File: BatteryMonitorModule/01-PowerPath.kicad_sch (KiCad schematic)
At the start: 22 parts, among them K1 G5LE-1, Q1 AO3401A, Q2 MMBT2222A, Q3 IRFZ44NPBF, Q3_DRV1 MMBT2222A

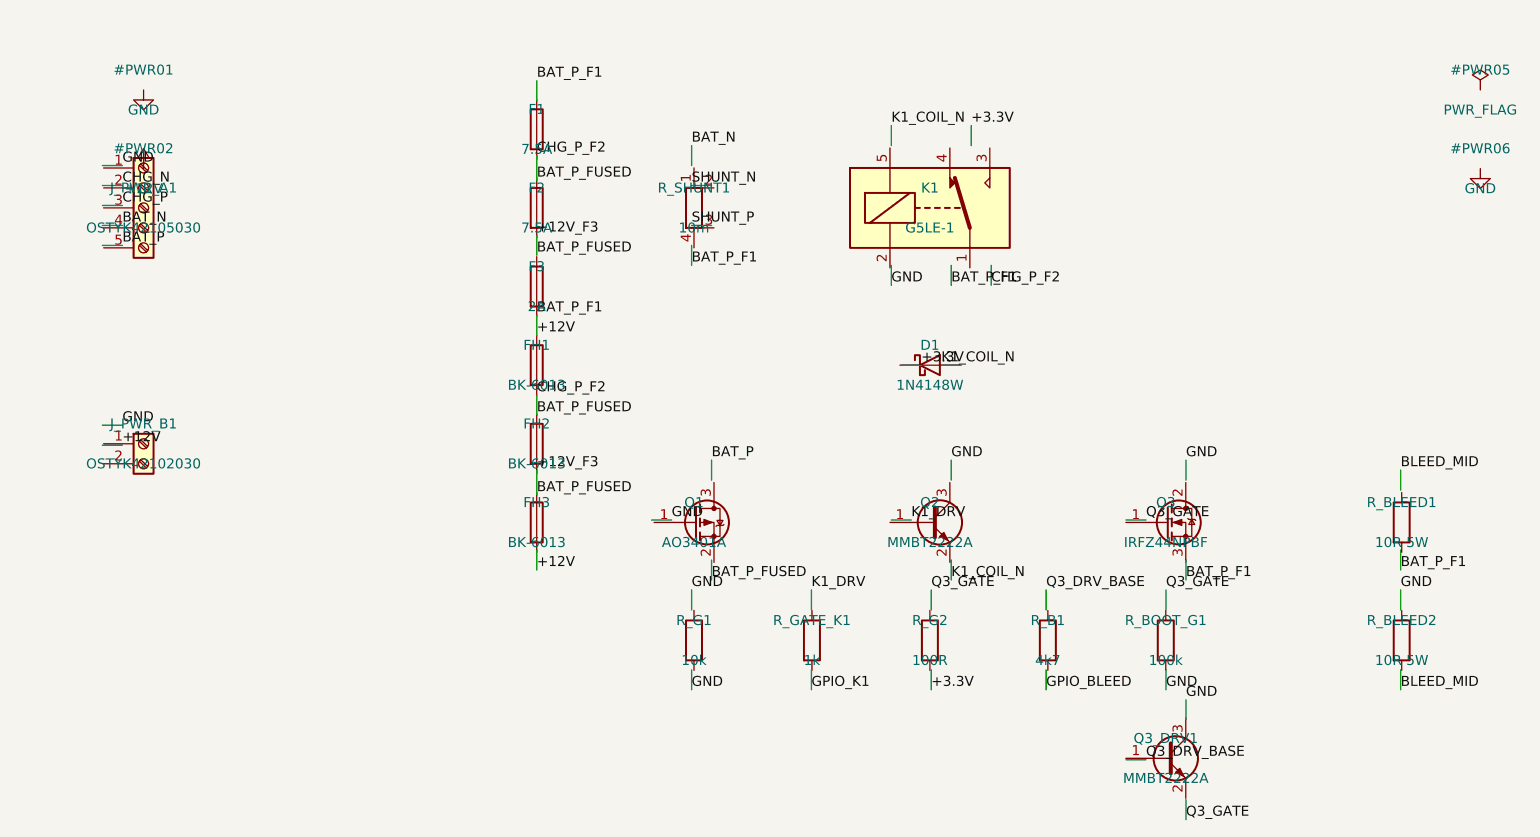
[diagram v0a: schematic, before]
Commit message: restructured project into BatteryMonitorModule/ directory with renamed sub-schematics
Co-Authored-By: Claude Opus 4.6 (1M context) <noreply@anthropic.com>
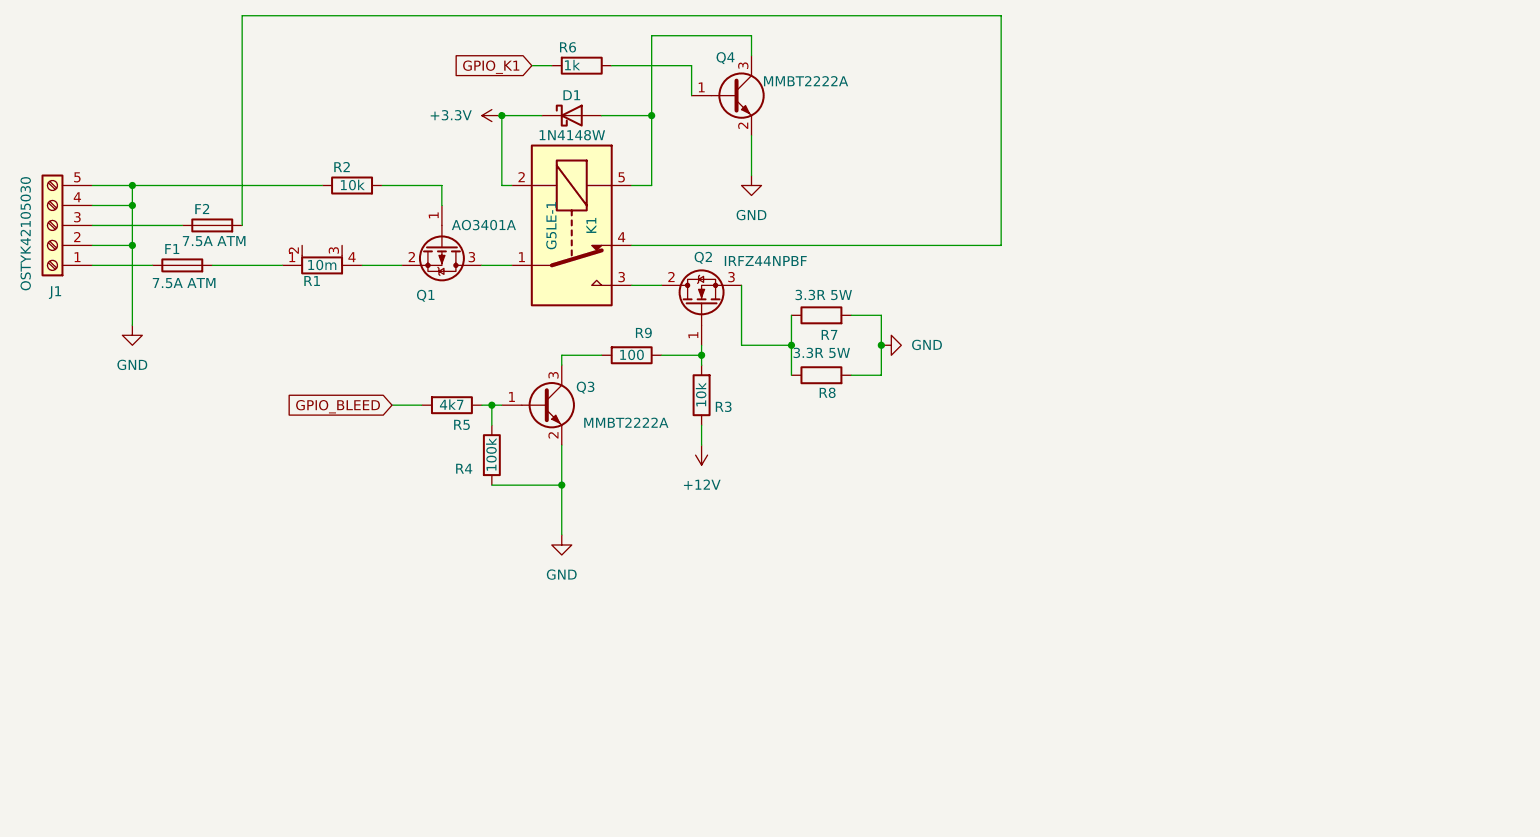
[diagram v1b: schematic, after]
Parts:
- removed F3: 2A, Fuse:Fuse_Blade_ATM_Mini, symbol Device:Fuse
- removed FH1, FH2, FH3: BK-6013, Fuse:Fuse_Blade_ATM_Mini, symbol Device:Fuse
- removed J_PWR_A1: OSTYK42105030, TerminalBlock_OnShore:TerminalBlock_OnShore_OSTTE050161_1x05_P5.08mm_Horizontal, symbol Connector:Screw_Terminal_01x05
- removed J_PWR_B1: OSTYK42102030, TerminalBlock_OnShore:TerminalBlock_OnShore_OSTTE020161_1x02_P5.08mm_Horizontal, symbol Connector:Screw_Terminal_01x02
- removed Q2, Q3_DRV1: MMBT2222A, Package_TO_SOT_SMD:SOT-23, symbol Transistor_BJT:MMBT2222A
- removed Q3: IRFZ44NPBF, Package_TO_SOT_THT:TO-220-3_Vertical, symbol Transistor_FET:IRLZ44N
- removed R_B1: 4k7, Resistor_SMD:R_0603_1608Metric, symbol Device:R
- removed R_BLEED1, R_BLEED2: 10R 5W, Resistor_THT:R_Axial_DIN0516_L15.5mm_D5.3mm_P22.86mm_Horizontal, symbol Device:R
- removed R_BOOT_G1: 100k, Resistor_SMD:R_0603_1608Metric, symbol Device:R
- removed R_G1: 10k, Resistor_SMD:R_0603_1608Metric, symbol Device:R
- removed R_G2: 100R, Resistor_SMD:R_0603_1608Metric, symbol Device:R
- removed R_GATE_K1: 1k, Resistor_SMD:R_0603_1608Metric, symbol Device:R
- removed R_SHUNT1: 10m, Resistor_SMD:R_2512_6332Metric, symbol Device:R_Shunt
- added J1: OSTYK42105030, symbol Connector:Screw_Terminal_01x05
- added Q2: IRFZ44NPBF, symbol Transistor_FET:IRLZ44N
- added Q3, Q4: MMBT2222A, symbol Transistor_BJT:MMBT2222A
- added R1: 10m, symbol Device:R_Shunt
- added R2, R3: 10k, symbol Device:R
- added R4: 100k, symbol Device:R
- added R5: 4k7, symbol Device:R
- added R6: 1k, symbol Device:R
- added R7, R8: 3.3R 5W, symbol Device:R
- added R9: 100, symbol Device:R
- D1: footprint Diode_SMD:D_SOD-123 -> (none); DK_PN 1N4148W-FDICT-ND -> (none); MPN 1N4148W-7-F -> (none)
- F1, F2: value 7.5A -> 7.5A ATM; footprint Fuse:Fuse_Blade_ATM_Mini -> (none); DK_PN F1197-ND -> (none); MPN ATM-7.5 -> (none)
- K1: footprint Relay_THT:Relay_SPDT_Omron-G5LE-1 -> (none); DK_PN Z682-ND -> (none); MPN G5LE-14-DC3 -> (none)
- Q1: footprint Package_TO_SOT_SMD:SOT-23 -> (none); DK_PN AO3401A-ND -> (none); MPN AO3401A -> (none)
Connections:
- net +12V: now also R3.1
- net +3.3V: now also D1.1 (K), K1.2
- net GND: now also J1.2 (Pin_2), J1.4 (Pin_4), J1.5 (Pin_5), Q3.2 (E), Q4.2 (E), R2.1, R4.2, R7.2, R8.2
- net GPIO_BLEED: now also R5.2
- net GPIO_K1: now also R6.2
- net at F2.1: now also J1.3 (Pin_3)
- net at F2.2: now also K1.4
- net at D1.2 (A): now also K1.5, Q4.3 (C)
- net at F1.1: now also J1.1 (Pin_1)
- net at F1.2: now also R1.1
- net at K1.1: now also Q1.3 (D)
- net at K1.3: now also Q2.2 (D)
- net at Q1.1 (G): now also R2.2
- net at Q1.2 (S): now also R1.4
- new net: Q2.1 (G), R3.2, R9.1
- new net: Q3.3 (C), R9.2
- new net: Q4.1 (B), R6.1
- new net: Q2.3 (S), R7.1, R8.1
- new net: Q3.1 (B), R4.1, R5.1
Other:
- title: (none) -> Battery Monitor Module — 01-PowerPath

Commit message: schematic annotation and component placement for power supply, MCU, and power path sheets
Added symbol libraries (AP63203, AP63205, MIC5219, TC2117), annotated
ref designators, and placed components via MCP server. Includes
fix_sheet_instances.py utility for restoring sheet_instances blocks.

Co-Authored-By: Claude Opus 4.6 (1M context) <noreply@anthropic.com>
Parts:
- added R13: 100R, symbol Device:R
- added R32: 10k, symbol Device:R
- added RT1: NTCG164BH103JT1, Resistor_SMD:R_0603_1608Metric, symbol Device:Thermistor_NTC
- D1: footprint (none) -> Diode_SMD:D_SOD-123
- Q1, Q3, Q4: footprint (none) -> Package_TO_SOT_SMD:SOT-23
- Q2: footprint (none) -> Package_TO_SOT_THT:TO-220-3_Vertical
- R1: footprint (none) -> Resistor_SMD:R_2512_6332Metric
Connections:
- net +3.3V: now also RT1.2
- net GND: now also R32.2
- net BAT_P_FUSED: now reaches K1.1, Q1.3 (D)
- net CHG_P_F2: now reaches F2.2, K1.4
- net SHUNT_P: now reaches R1.2
- net SHUNT_N: now reaches R1.3
- new net: R13.1, R32.1, RT1.1
- new net ADC_NTC: R13.2
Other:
- moved on the sheet: R2

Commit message: updated all schematics — IO sheet wiring, MCU connections, power supply refinements, custom footprints
Co-Authored-By: Claude Opus 4.6 (1M context) <noreply@anthropic.com>
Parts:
- F1, F2: footprint (none) -> Fuse:FuseHolder_Blade_ATO_Littelfuse_FLR_178.6165
- J1: footprint (none) -> TerminalBlock_Phoenix:TerminalBlock_Phoenix_MKDS-1,5-5-5.08_1x05_P5.08mm_Horizontal
- K1: footprint (none) -> Relay_THT:Relay_SPDT_Omron-G5LE-1
- R13, R2, R3, R32, R4, R5, R6, R9: footprint (none) -> Resistor_SMD:R_0603_1608Metric
- R7, R8: footprint (none) -> BatteryMonitorModule_Custom:YAG_SQP500_YAG
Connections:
- net GND: no longer R7.2
- net at Q2.3 (S), R7.1: no longer R8.1
- new net: R7.2, R8.1
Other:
- moved on the sheet: R8

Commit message: added connector footprints and power path updates
New custom footprints: OSTYK screw terminals, KF8500 connectors, USB4085-GF-A.
Power path schematic updates and project library references.

Co-Authored-By: Claude Opus 4.6 (1M context) <noreply@anthropic.com>
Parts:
- J1: footprint TerminalBlock_Phoenix:TerminalBlock_Phoenix_MKDS-1,5-5-5.08_1x05_P5.08mm_Horizontal -> BatteryMonitorModule_Custom:OSTYK42105030
- R1: footprint Resistor_SMD:R_2512_6332Metric -> Resistor_SMD:R_Shunt_Vishay_WSK2512_6332Metric_T2.21mm
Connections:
- net CRG+: now reaches F2.1, J1.3 (Pin_3)
- net BAT+: now reaches F1.1, J1.1 (Pin_1)
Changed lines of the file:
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@@
+		)
+	)
+	(label "BAT-"
+		(at 29.21 48.26 0)
+		(effects
+			(font
+				(size 1.27 1.27)
+			)
+			(justify left bottom)
+		)
+	)
+	(label "CRG-"
+		(at 29.21 43.18 0)
+		(effects
+			(font
+				(size 1.27 1.27)
+			)
+			(justify left bottom)
+		)
+	)
+	(label "CRG+"
+		(at 29.21 45.72 0)
+		(effects
+			(font
+				(size 1.27 1.27)
+			)
+			(justify left bottom)
+		)
+	)
+	(label "PE GND"
+		(at 29.21 40.64 0)
+		(effects
+			(font
+				(size 1.27 1.27)
+			)
+			(justify left bottom)
+		)
+	)
+	(label "BAT+"
+		(at 29.21 50.8 0)
+		(effects
+			(font
+				(size 1.27 1.27)
+			)
+			(justify left bottom)
 		)
 	)
@@
 			)
 		)
-		(property "Footprint" "Resistor_SMD:R_2512_6332Metric"
+		(property "Footprint" "Resistor_SMD:R_Shunt_Vishay_WSK2512_6332Metric_T2.21mm"
 			(at 57.15 50.8 0)
 			(hide yes)
@@
 			)
 		)
-		(property "Footprint" "TerminalBlock_Phoenix:TerminalBlock_Phoenix_MKDS-1,5-5-5.08_1x05_P5.08mm_Horizontal"
+		(property "Footprint" "BatteryMonitorModule_Custom:OSTYK42105030"
 			(at 22.86 45.72 0)
 			(hide yes)
